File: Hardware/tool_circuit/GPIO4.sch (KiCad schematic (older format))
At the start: 1 part, among them J2 Conn_01x03_Female

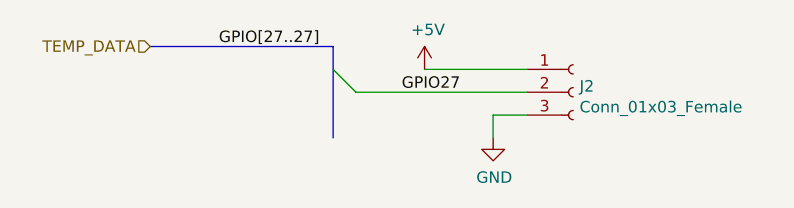
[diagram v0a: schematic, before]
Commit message: Tool Circuit schematic updates
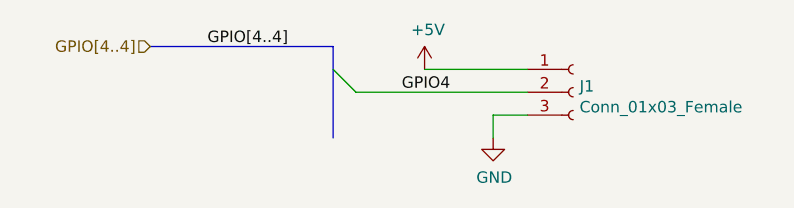
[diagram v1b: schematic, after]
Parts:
- renumbered J2 to J1
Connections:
- net GPIO27 renamed GPIO4
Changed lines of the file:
@@
 $Descr A4 11693 8268
 encoding utf-8
-Sheet 8 8
+Sheet 6 8
 Title ""
 Date ""
@@
 $EndDescr
 $Comp
-L Connector:Conn_01x03_Female J2
+L Connector:Conn_01x03_Female J1
 U 1 1 614AEC17
 P 5700 3500
-F 0 "J2" H 5728 3526 50  0000 L CNN
+F 0 "J1" H 5728 3526 50  0000 L CNN
 F 1 "Conn_01x03_Female" H 5728 3435 50  0000 L CNN
 F 2 "Connector_PinHeader_2.54mm:PinHeader_1x03_P2.54mm_Vertical" H 5700 3500 50  0001 C CNN
@@
 $EndComp
 $Comp
-L power:GND #PWR011
+L power:GND #PWR09
 U 1 1 614AF32D
 P 5350 3700
-F 0 "#PWR011" H 5350 3450 50  0001 C CNN
+F 0 "#PWR09" H 5350 3450 50  0001 C CNN
 F 1 "GND" H 5355 3527 50  0000 C CNN
 F 2 "" H 5350 3700 50  0001 C CNN
@@
 	5350 3600 5350 3700
 $Comp
-L power:+5V #PWR010
+L power:+5V #PWR08
 U 1 1 614AFBC4
 P 5050 3400
-F 0 "#PWR010" H 5050 3250 50  0001 C CNN
+F 0 "#PWR08" H 5050 3250 50  0001 C CNN
 F 1 "+5V" H 5065 3573 50  0000 C CNN
 F 2 "" H 5050 3400 50  0001 C CNN
@@
 	5050 3400 5500 3400
 Text HLabel 3850 3300 0    50   Input ~ 0
-TEMP_DATA
+GPIO[4..4]
 Wire Bus Line
 	3850 3300 4650 3300
@@
 	4650 3300 4650 3700
 Text Label 4950 3500 0    50   ~ 0
-GPIO27
-Text Label 4150 3300 0    50   ~ 0
-GPIO[27..27]
+GPIO4
+Text Label 4100 3300 0    50   ~ 0
+GPIO[4..4]
 $EndSCHEMATC
